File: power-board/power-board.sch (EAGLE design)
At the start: 11 parts, among them J1 1X2-3.5MM, J2 1X2-3.5MM, J3 1X2-3.5MM, J4 1X2-3.5MM

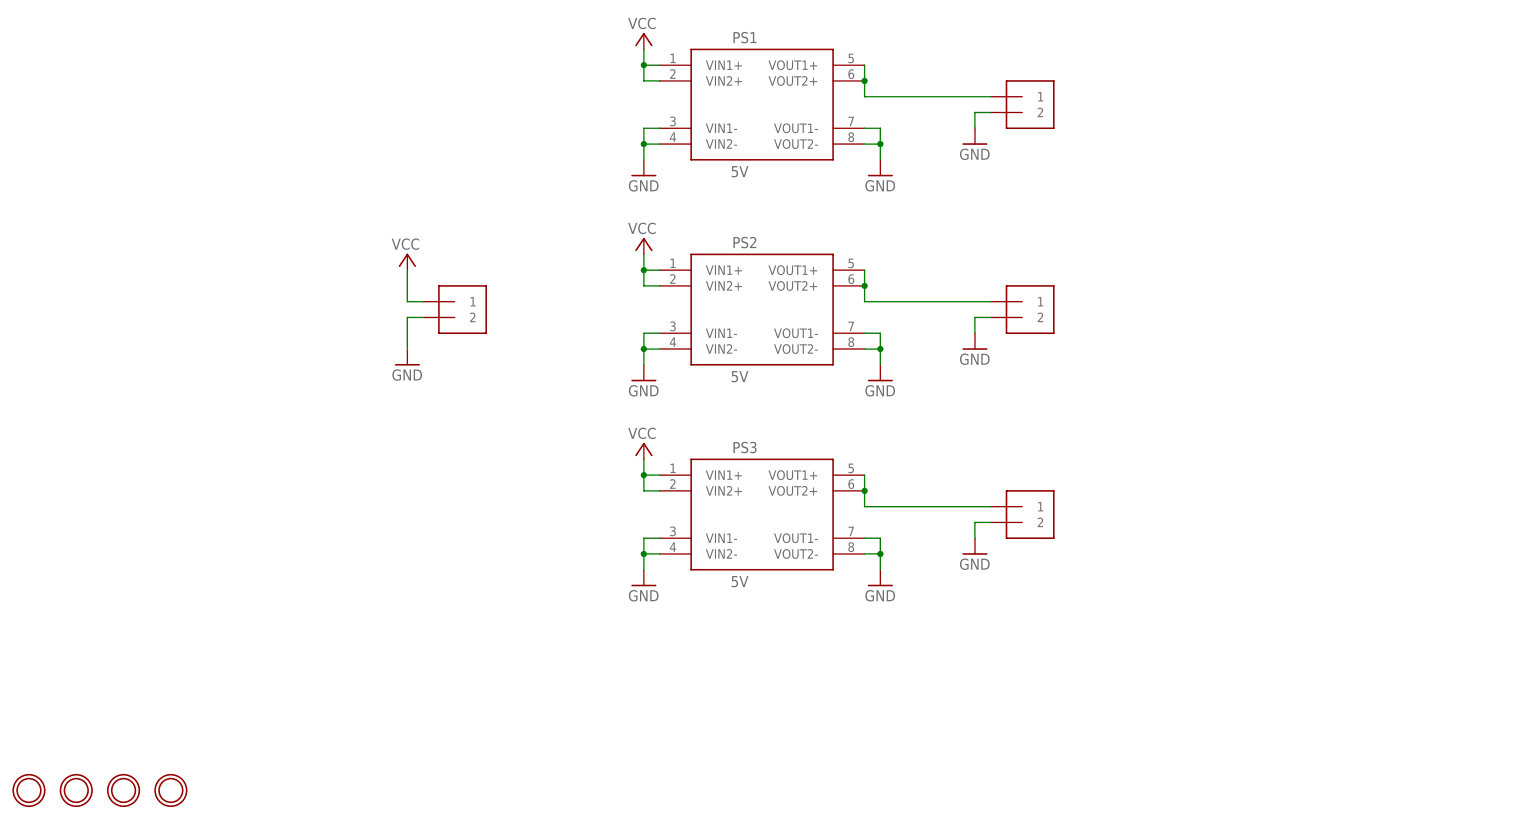
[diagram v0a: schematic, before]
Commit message: Add Power-Hat
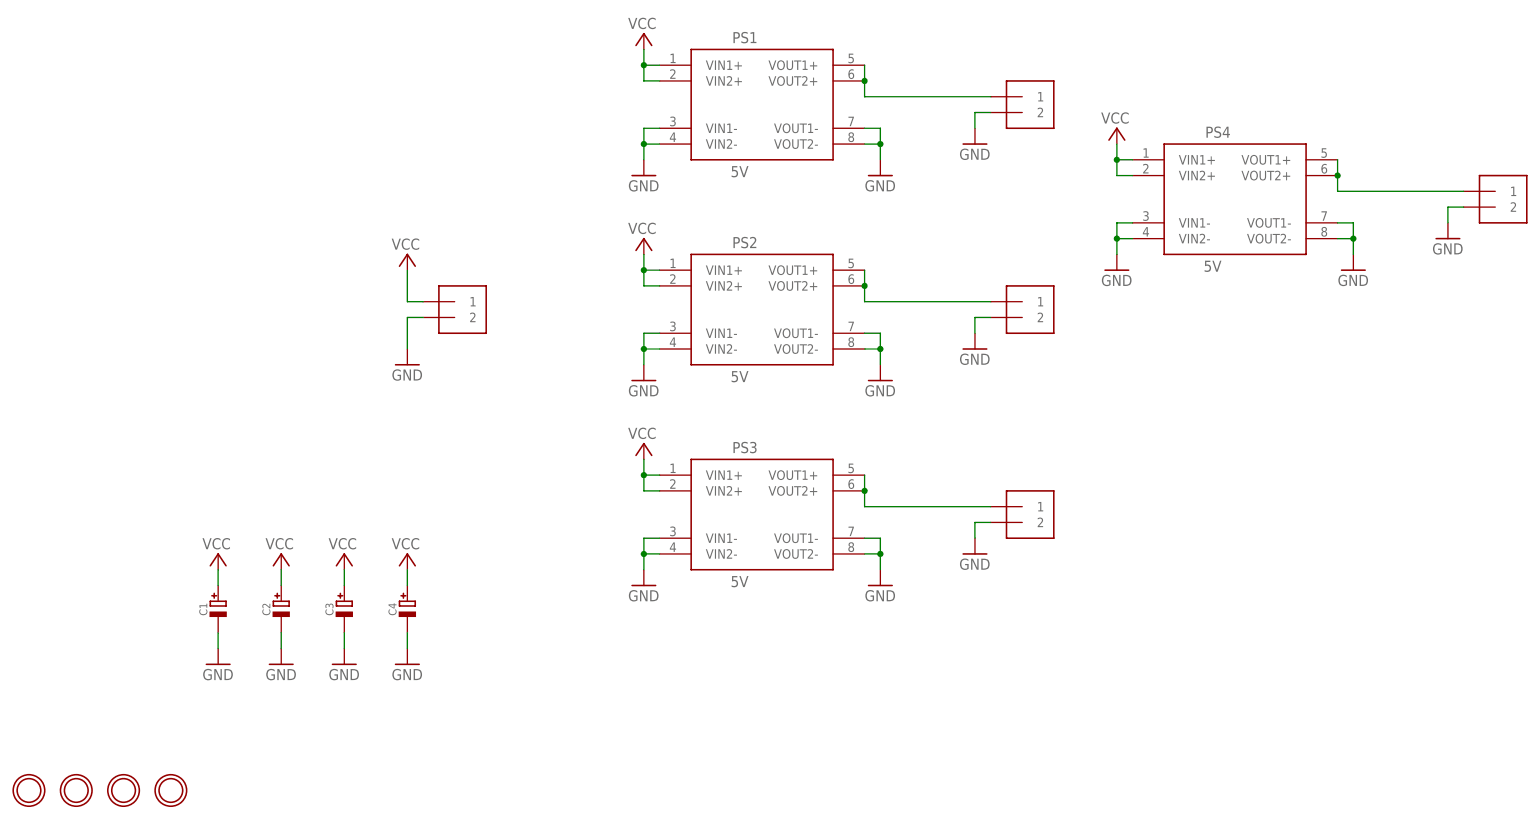
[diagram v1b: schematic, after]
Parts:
- added C1, C2, C3, C4: (no value), sanisimov:CAP_ELECTROLYTICPTH_3.5MMGRID_8MMDIA
- added J6: (no value), sanisimov:WR_TBL_1X2-3.5MM
- added PS4: 5V, sanisimov:K8801MODULE
- J1, J2, J3, J4: value 1X2-3.5MM -> (none); device adafruit:1X2-3.5MM -> sanisimov:WR_TBL_1X2-3.5MM
- U$1, U$2, U$3, U$4: value MICROBUILDER_MOUNTINGHOLE2.5 -> MOUNTINGHOLE3.0THIN; device Adafruit DRV8871:MICROBUILDER_MOUNTINGHOLE2.5 -> sanisimov:MOUNTINGHOLE3.0THIN
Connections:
- new net N$1: J6.1, PS4.VOUT1+, PS4.VOUT2+
- net GND: now also C1.-, C2.-, C3.-, C4.-, J6.2, PS4.VIN1-, PS4.VIN2-, PS4.VOUT1-, PS4.VOUT2-
- net VCC: now also C1.+, C2.+, C3.+, C4.+, PS4.VIN1+, PS4.VIN2+

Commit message: Publish v1.0.0 Power Board and Power Bridge
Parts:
- removed C2, C3, C4: (no value), sanisimov:CAP_ELECTROLYTICPTH_3.5MMGRID_8MMDIA
- removed J1, J2, J3, J4, J6: (no value), sanisimov:WR_TBL_1X2-3.5MM
- removed PS2, PS3, PS4: 5V, sanisimov:K8801MODULE
- removed U$1, U$4: MOUNTINGHOLE3.0THIN, sanisimov:MOUNTINGHOLE3.0THIN
- added X1: CON-FE02-1, _Library.b1f76137-4d0f-4ce2-9703-0cd83550450f.flbr:CON-FE02-1
- added X2: CON-FE02-2HDRVR4W64P254_2X2, _Library.b1f76137-4d0f-4ce2-9703-0cd83550450f.flbr:CON-FE02-2HDRVR4W64P254_2X2
- added X3, X4: CON-MA02-1, _Library.b1f76137-4d0f-4ce2-9703-0cd83550450f.flbr:CON-MA02-1
- C1: value (none) -> CAP_ELECTROLYTIC; device sanisimov:CAP_ELECTROLYTICPTH_3.5MMGRID_8MMDIA -> _Library.b1f76137-4d0f-4ce2-9703-0cd83550450f.flbr:CAP_ELECTROLYTIC
- PS1: value 5V -> (none); device sanisimov:K8801MODULE -> _Library.b1f76137-4d0f-4ce2-9703-0cd83550450f.flbr:K8801MODULE
- U$2, U$3: value MOUNTINGHOLE3.0THIN -> MOUNTINGHOLE2.7_THICK; device sanisimov:MOUNTINGHOLE3.0THIN -> _Library.b1f76137-4d0f-4ce2-9703-0cd83550450f.flbr:MOUNTINGHOLE2.7_THICK
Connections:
- removed net N$3: J3.1, PS2.VOUT1+, PS2.VOUT2+
- removed net N$5: J4.1, PS3.VOUT1+, PS3.VOUT2+
- removed net N$7: J2.1, PS1.VOUT1+, PS1.VOUT2+
- removed net VCC: C1.+, C2.+, C3.+, C4.+, J1.1, PS1.VIN1+, PS1.VIN2+, PS2.VIN1+, PS2.VIN2+, PS3.VIN1+, PS3.VIN2+, PS4.VIN1+, PS4.VIN2+
- new net VIN: C1.+, PS1.VIN1+, PS1.VIN2+, X1.1, X3.2, X4.4
- net GND: now also X1.3, X2.1, X2.2, X3.4, X4.2; no longer C2.-, C3.-, C4.-, J1.2, J2.2, J3.2, J4.2, J6.2, PS2.VIN1-, PS2.VIN2-, PS2.VOUT1-, PS2.VOUT2-, PS3.VIN1-, PS3.VIN2-, PS3.VOUT1-, PS3.VOUT2-, PS4.VIN1-, PS4.VIN2-, PS4.VOUT1-, PS4.VOUT2-
- net N$1: now also PS1.VOUT1+, PS1.VOUT2+, X2.3, X2.4; no longer J6.1, PS4.VOUT1+, PS4.VOUT2+
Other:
- note added: "Mounting holes"
- moved on the sheet: C1, NAME
